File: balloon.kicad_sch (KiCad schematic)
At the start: 13 parts, among them SW1 SW_Push, U1 STM32L431RBTx, Y1 Crystal

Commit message: make board
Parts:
- added C1, C12, C13, C2: 100n, Capacitor_SMD:C_0603_1608Metric_Pad1.08x0.95mm_HandSolder, symbol Device:C
- added C14, C17: 4.7u, Capacitor_SMD:C_0603_1608Metric_Pad1.08x0.95mm_HandSolder, symbol Device:C
- added C5, C6: C, Capacitor_SMD:C_0603_1608Metric_Pad1.08x0.95mm_HandSolder, symbol Device:C
- added D1, D2: SK6812MINI, LED_SMD:LED_SK6812MINI_PLCC4_3.5x3.5mm_P1.75mm, symbol LED:SK6812MINI
- added J1: USB_B_Micro, Connector_USB:USB_Micro-B_Molex_47346-0001, symbol Connector:USB_B_Micro
- added J2, J3: Conn_01x06_Socket, Connector_PinHeader_2.54mm:PinHeader_1x06_P2.54mm_Vertical, symbol Connector:Conn_01x06_Socket
- added J4: Conn_01x02_Socket, Connector_PinHeader_2.54mm:PinHeader_1x02_P2.54mm_Vertical, symbol Connector:Conn_01x02_Socket
- added J5: Writing Connector, Connector_PinSocket_2.54mm:PinSocket_1x06_P2.54mm_Vertical, symbol Connector:Conn_01x06_Pin
- added R3: 10k, Resistor_SMD:R_0603_1608Metric_Pad0.98x0.95mm_HandSolder, symbol Device:R
- added R33, R34, R4: 2.2k, Resistor_SMD:R_0603_1608Metric_Pad0.98x0.95mm_HandSolder, symbol Device:R
- added U1: CH340N, Package_SO:MSOP-10_3x3mm_P0.5mm, symbol balloon_lib:CH340N
- added U2: Qwiic-SAM-M8Q, balloon:Qwiic_SAM-M8Q, symbol balloon_lib:Qwiic-SAM-M8Q
- added U3: AE_BME280, balloon:AE_BNE280, symbol balloon_lib:BME280
- added U4: AE_BNO055, balloon:AE-BNO055, symbol balloon_lib:BNO055
- added Y1: Crystal, Crystal:Crystal_C38-LF_D3.0mm_L8.0mm_Vertical, symbol Device:Crystal
- C10: renamed from C5; footprint (none) -> Capacitor_SMD:C_0603_1608Metric_Pad1.08x0.95mm_HandSolder
- C11: renamed from C9; footprint (none) -> Capacitor_SMD:C_0603_1608Metric_Pad1.08x0.95mm_HandSolder
- C3: renamed from C2; footprint (none) -> Capacitor_SMD:C_0603_1608Metric_Pad1.08x0.95mm_HandSolder
- C4: renamed from C3; footprint (none) -> Capacitor_SMD:C_0603_1608Metric_Pad1.08x0.95mm_HandSolder
- C7, C8: footprint (none) -> Capacitor_SMD:C_0603_1608Metric_Pad1.08x0.95mm_HandSolder; now not fitted
- C9: renamed from C4; footprint (none) -> Capacitor_SMD:C_0603_1608Metric_Pad1.08x0.95mm_HandSolder
- R1: renamed from R28; footprint (none) -> Resistor_SMD:R_0603_1608Metric_Pad0.98x0.95mm_HandSolder
- R2: renamed from R29; footprint (none) -> Resistor_SMD:R_0603_1608Metric_Pad0.98x0.95mm_HandSolder
- R5: renamed from R30; footprint (none) -> Resistor_SMD:R_0603_1608Metric_Pad0.98x0.95mm_HandSolder
- SW1: value SW_Push -> DTS-63-F-N-V-RED; footprint (none) -> Button_Switch_THT:SW_PUSH_6mm
- Y2: renamed from Y1; footprint (none) -> Crystal:Crystal_C38-LF_D3.0mm_L8.0mm_Vertical; now not fitted
- renumbered U1 to U5
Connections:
- net VMEM is gone; now on net +3V3: U5.1 (VBAT)
- net +3V3: now also C12.1, C14.1, C17.1, C2.1, D1.4 (VDD), D2.4 (VDD), J4.1 (Pin_1), R33.1, R34.1; no longer R1.1, R2.1
- net BNO055_RESET: now also U4.5 (RESET_N)
- net GND1: now also C1.2, C12.2, C13.2, C14.2, C17.2, C2.2, C5.1, C6.2, D1.2 (VSS), D2.2 (VSS), J1.5 (GND), J1.6 (Shield), J5.3 (Pin_3), R3.2, R4.2, U1.3 (GND), U2.13 (GND), U2.14 (GND), U2.5 (GND), U3.2 (GND), U4.2 (GND), U4.7 (GND); no longer SW1.1
- net GPS_INT: now also U2.4 (INT)
- net GPS_RESET: now also U2.2 (RST_N)
- net GPS_SAFE: now also U2.3 (SAFE_N)
- net I2C1_SCL: now also U4.4 (SCL/RX)
- net I2C1_SDA: now also U4.3 (SDA/TX)
- net LPTIM1_IN: now also U2.1 (PPS)
- net SPI1_CLK: now also U3.6 (SCK/SCL)
- net SPI1_MISO: now also U3.5 (MISO/GND)
- net SPI1_MOSI: now also U3.4 (MOSI/SDA)
- net SPI1_SS: now also U3.3 (CSB/VDD)
- net USART1_RX: now also U5.43 (PA10); no longer U5.59 (PB7)
- net USART3_RX: now also U2.10 (TXD)
- net USART3_TX: now also U2.11 (RXD)
- net NRST: now reaches R5.2, SW1.2, U5.7 (NRST)
- net NRST: now also C13.1, J5.5 (Pin_5)
- net PA0: now reaches U5.14 (PA0)
- net PA0: now also J3.3 (Pin_3)
- net USART2_TX: now reaches U5.16 (PA2)
- net USART2_TX: now also U1.7 (RXD)
- net USART2_RX: now reaches U5.17 (PA3)
- net USART2_RX: now also U1.6 (TXD)
- net CTRL_SENSE: now reaches U5.21 (PA5)
- net CTRL_COMM: now reaches U5.22 (PA6)
- net PA7: now reaches U5.23 (PA7)
- net PA7: now also J3.4 (Pin_4)
- net PB0: now reaches U5.26 (PB0)
- net PB0: now also J3.6 (Pin_6)
- net PB2: now reaches U5.28 (PB2)
- net PB2: now also J2.1 (Pin_1)
- net I2C2_SCL: now reaches U5.29 (PB10)
- net I2C2_SCL: now also R33.2
- net I2C2_SDA: now reaches U5.30 (PB11)
- net I2C2_SDA: now also R34.2
- net PB12: now reaches U5.33 (PB12)
- net PB12: now also J2.3 (Pin_3)
- net PB13: now reaches U5.34 (PB13)
- net PB13: now also J2.4 (Pin_4)
- net PB14: now reaches U5.35 (PB14)
- net PB14: now also J2.5 (Pin_5)
- net PB15: now reaches U5.36 (PB15)
- net PB15: now also J2.6 (Pin_6)
- net LED_OUT: now reaches U5.41 (PA8)
- net LED_OUT: now also D1.3 (DIN)
- net SWDIO: now reaches U5.46 (PA13)
- net SWDIO: now also J5.4 (Pin_4)
- net SWCLK: now reaches U5.49 (PA14)
- net SWCLK: now also J5.2 (Pin_2)
- net OSC_IN: now reaches U5.5 (PH0)
- net OSC_IN: now also C5.2, Y1.2
- net PA15: now reaches U5.50 (PA15)
- net PA15: now also J3.5 (Pin_5)
- net SWO: now reaches U5.55 (PB3)
- net SWO: now also J5.6 (Pin_6)
- net OSC_OUT: now reaches U5.6 (PH1)
- net OSC_OUT: now also C6.1, Y1.1
- net BOOT0: now reaches U5.60 (PH3)
- net BOOT0: now also J4.2 (Pin_2), R3.1
- net PC0: now reaches U5.8 (PC0)
- net PC0: now also J3.1 (Pin_1)
- net PC1: now reaches U5.9 (PC1)
- net PC1: now also J3.2 (Pin_2)
- new net: J1.2 (D-), U1.2 (UD-)
- new net: J1.3 (D+), U1.1 (UD+)
- new net: R4.1, SW1.1
- new net: C1.1, U1.8 (V3)
- new net: D1.1 (DOUT), D2.3 (DIN)
- new net +3.3V: J5.1 (Pin_1)
- new net PB7: J2.2 (Pin_2), U5.59 (PB7)
- new net PowerSource/5VIN: J1.1 (VBUS), U1.5 (~{CTS})
- new net PowerSource/VSENSE: R1.1, R2.1, U2.12 (3V3), U2.6 (3v3), U3.1 (VDD), U4.1 (VIN)
- no-connect marks 27 -> 8
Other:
- removed sheet BME280
- removed sheet BNO055
- removed sheet GPS
- sheet PowerSource ports: added 5VIN, CTRL_COMM, CTRL_SENSE, SCL, SDA, VCOMM, VSENSE, V_DEF; removed none
- sheet RM92A ports: added VIN; removed none
- sheet SDCard ports: added VIN; removed none
- moved on the sheet: C10, C11, C3, C4, C9, R1, R2, R5, SW1, U5

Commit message: replace PCB
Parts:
- added H1, H2, H3: MountingHole, MountingHole:MountingHole_3.2mm_M3_ISO7380, symbol Mechanical:MountingHole
- added J7: Conn_01x06_Socket, Connector_PinHeader_2.54mm:PinHeader_1x06_P2.54mm_Vertical, symbol Connector:Conn_01x06_Socket
- U1: footprint Package_SO:MSOP-10_3x3mm_P0.5mm -> Package_SO:SOP-8_3.9x4.9mm_P1.27mm
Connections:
- net +3V3: now also J3.6 (Pin_6), J7.6 (Pin_6)
- net GND1: now also J2.6 (Pin_6), J3.5 (Pin_5), J7.5 (Pin_5)
- net PA0: now also J2.3 (Pin_3); no longer J3.3 (Pin_3)
- net PA15: no longer J3.5 (Pin_5)
- net PA7: now also J2.4 (Pin_4); no longer J3.4 (Pin_4)
- net PB0: now also J2.5 (Pin_5); no longer J3.6 (Pin_6)
- net PB12 renamed SPI2_NSS
- net SPI2_NSS: now also J7.1 (Pin_1); no longer J2.3 (Pin_3)
- net PB13 renamed SPI2_SCK
- net SPI2_SCK: now also J7.4 (Pin_4); no longer J2.4 (Pin_4)
- net PB14 renamed SPI2_MISO
- net SPI2_MISO: now also J7.3 (Pin_3); no longer J2.5 (Pin_5)
- net PB15 renamed SPI2_MOSI
- net SPI2_MOSI: now also J7.2 (Pin_2); no longer J2.6 (Pin_6)
- net PC0 renamed I2C3_SCL
- net I2C3_SCL: now also J3.2 (Pin_2); no longer J3.1 (Pin_1)
- net PC1 renamed I2C3_SDA
- net I2C3_SDA: now also J3.1 (Pin_1); no longer J3.2 (Pin_2)
- no-connect marks 8 -> 10

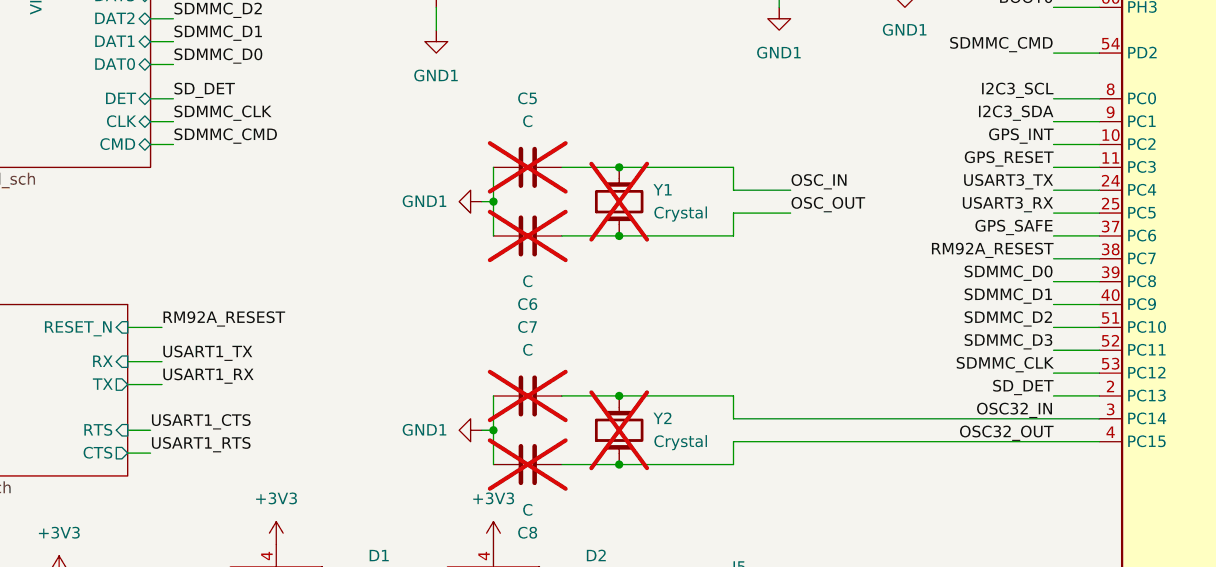
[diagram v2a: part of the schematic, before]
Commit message: add stmcube
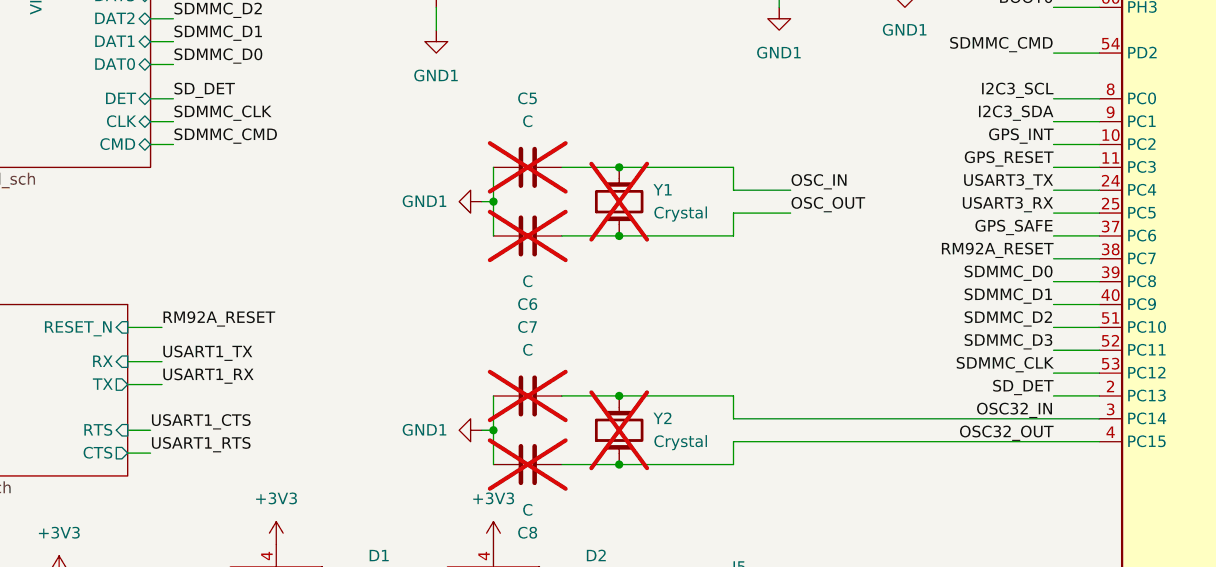
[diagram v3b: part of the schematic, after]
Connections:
- net RM92A_RESEST renamed RM92A_RESET

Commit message: change gnss
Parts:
- removed U2: Qwiic-SAM-M8Q, balloon:Qwiic_SAM-M8Q, symbol balloon_lib:Qwiic-SAM-M8Q
- added D7: D, Diode_SMD:D_SMA_Handsoldering, symbol Device:D
- added H4: MountingHole, MountingHole:MountingHole_3.2mm_M3_ISO7380, symbol Mechanical:MountingHole
- added R36: 1k, Resistor_SMD:R_0603_1608Metric_Pad0.98x0.95mm_HandSolder, symbol Device:R
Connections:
- net PowerSource/VSENSE renamed MAX-M10S/VIN
- net MAX-M10S/VIN: now also R36.2
- new net: D7.2 (A), R36.1
- new net MAX-M10S/VBKUP: D7.1 (K)
- no-connect marks 10 -> 8
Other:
- added sheet MAX-M10S (maxm10-s.kicad_sch)

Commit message: set gerber
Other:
- note added: "とりあえずブリッジさせる"
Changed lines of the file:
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@@
     (stroke (width 0) (type default))
+  )
+  (text "とりあえずブリッジさせる" (at 67.31 60.96 0)
+    (effects (font (size 1.27 1.27)) (justify left bottom))
   )
   (label "I2C1_SDA" (at 266.7 128.27 0) (fields_autoplaced)

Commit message: change schematics
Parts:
- H1, H2, H3, H4: footprint MountingHole:MountingHole_3.2mm_M3_ISO7380 -> MountingHole:MountingHole_3.2mm_M3_ISO7380_Pad_TopBottom; symbol Mechanical:MountingHole -> Mechanical:MountingHole_Pad
- SW1: footprint Button_Switch_THT:SW_PUSH_6mm -> Button_Switch_SMD:SW_SPST_PTS645
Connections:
- net GND1: now also H1.1, H2.1, H3.1, H4.1
- net USBD-: now reaches J1.2 (D-), U1.2 (UD-)
- net USBD+: now reaches J1.3 (D+), U1.1 (UD+)
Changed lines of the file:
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@@
   (junction (at 68.58 64.77) (diameter 0) (color 0 0 0 0)
   )
+  (junction (at 148.59 172.72) (diameter 0) (color 0 0 0 0)
+  )
+  (junction (at 148.59 167.64) (diameter 0) (color 0 0 0 0)
+  )
   (junction (at 73.66 171.45) (diameter 0) (color 0 0 0 0)
   )
@@
   )
   (junction (at 176.53 97.79) (diameter 0) (color 0 0 0 0)
+  )
+  (junction (at 148.59 162.56) (diameter 0) (color 0 0 0 0)
   )
   (junction (at 48.26 15.24) (diameter 0) (color 0 0 0 0)
@@
     (stroke (width 0) (type default))
   )
+  (wire (pts (xy 152.4 172.72) (xy 148.59 172.72))
+    (stroke (width 0) (type default))
+  )
   (wire (pts (xy 189.23 92.71) (xy 189.23 90.17))
     (stroke (width 0) (type default))
@@
     (stroke (width 0) (type default))
   )
+  (wire (pts (xy 148.59 162.56) (xy 148.59 157.48))
+    (stroke (width 0) (type default))
+  )
   (wire (pts (xy 114.3 195.58) (xy 116.84 195.58))
     (stroke (width 0) (type default))
@@
     (stroke (width 0) (type default))
   )
+  (wire (pts (xy 148.59 167.64) (xy 148.59 162.56))
+    (stroke (width 0) (type default))
+  )
   (wire (pts (xy 247.65 54.61) (xy 247.65 57.15))
     (stroke (width 0) (type default))
@@
     (stroke (width 0) (type default))
   )
+  (wire (pts (xy 148.59 172.72) (xy 148.59 167.64))
+    (stroke (width 0) (type default))
+  )
   (wire (pts (xy 247.65 20.32) (xy 260.35 20.32))
     (stroke (width 0) (type default))
@@
     (effects (font (size 1.27 1.27)) (justify right bottom))
   )
+  (label "USBD-" (at 29.21 35.56 0) (fields_autoplaced)
+    (effects (font (size 1.27 1.27)) (justify left bottom))
+  )
   (label "USART1_RTS" (at 266.7 92.71 0) (fields_autoplaced)
     (effects (font (size 1.27 1.27)) (justify left bottom))
@@
   )
   (label "NRST" (at 215.9 62.23 0) (fields_autoplaced)
+    (effects (font (size 1.27 1.27)) (justify left bottom))
+  )
+  (label "USBD+" (at 29.21 33.02 0) (fields_autoplaced)
     (effects (font (size 1.27 1.27)) (justify left bottom))
   )
@@
       (effects (font (size 1.27 1.27)))
     )
-    (property "Footprint" "Button_Switch_THT:SW_PUSH_6mm" (at 199.39 57.15 0)
+    (property "Footprint" "Button_Switch_SMD:SW_SPST_PTS645" (at 199.39 57.15 0)
       (effects (font (size 1.27 1.27)) hide)
     )
@@
     )
   )
-  (symbol (lib_id "Mechanical:MountingHole") (at 146.05 162.56 0) (unit 1)
-    (in_bom yes) (on_board yes) (dnp no) (fields_autoplaced)
-    (property "Reference" "H2" (at 148.59 161.3479 0)
-      (effects (font (size 1.27 1.27)) (justify left))
-    )
-    (property "Value" "MountingHole" (at 148.59 163.7721 0)
-      (effects (font (size 1.27 1.27)) (justify left))
-    )
-    (property "Footprint" "MountingHole:MountingHole_3.2mm_M3_ISO7380" (at 146.05 162.56 0)
+  (symbol (lib_id "Mechanical:MountingHole_Pad") (at 146.05 162.56 90) (unit 1)
+    (in_bom yes) (on_board yes) (dnp no)
+    (property "Reference" "H2" (at 140.97 161.29 90)
+      (effects (font (size 1.27 1.27)))
+    )
+    (property "Value" "MountingHole" (at 135.89 163.83 90)
+      (effects (font (size 1.27 1.27)))
+    )
+    (property "Footprint" "MountingHole:MountingHole_3.2mm_M3_ISO7380_Pad_TopBottom" (at 146.05 162.56 0)
       (effects (font (size 1.27 1.27)) hide)
     )
@@
       (effects (font (size 1.27 1.27)) hide)
     )
+    (pin "1")
     (instances
       (project "balloon"
@@
     )
   )
+  (symbol (lib_id "power:GND1") (at 152.4 172.72 0) (unit 1)
+    (in_bom yes) (on_board yes) (dnp no) (fields_autoplaced)
+    (property "Reference" "#PWR061" (at 152.4 179.07 0)
+      (effects (font (size 1.27 1.27)) hide)
+    )
+    (property "Value" "GND1" (at 152.4 177.8 0)
+      (effects (font (size 1.27 1.27)))
+    )
+    (property "Footprint" "" (at 152.4 172.72 0)
+      (effects (font (size 1.27 1.27)) hide)
+    )
+    (property "Datasheet" "" (at 152.4 172.72 0)
+      (effects (font (size 1.27 1.27)) hide)
+    )
+    (pin "1")
+    (instances
+      (project "balloon"
+        (path "/390c33b5-3f3b-4c86-a202-e8d785058178"
+          (reference "#PWR061") (unit 1)
+        )
+      )
+    )
+  )
   (symbol (lib_id "Device:C") (at 166.37 97.79 270) (mirror x) (unit 1)
     (in_bom yes) (on_board yes) (dnp yes)
@@
     )
   )
-  (symbol (lib_id "Mechanical:MountingHole") (at 146.05 172.72 0) (unit 1)
-    (in_bom yes) (on_board yes) (dnp no) (fields_autoplaced)
-    (property "Reference" "H4" (at 148.59 171.5079 0)
-      (effects (font (size 1.27 1.27)) (justify left))
-    )
-    (property "Value" "MountingHole" (at 148.59 173.9321 0)
-      (effects (font (size 1.27 1.27)) (justify left))
-    )
-    (property "Footprint" "MountingHole:MountingHole_3.2mm_M3_ISO7380" (at 146.05 172.72 0)
+  (symbol (lib_id "Mechanical:MountingHole_Pad") (at 146.05 172.72 90) (unit 1)
+    (in_bom yes) (on_board yes) (dnp no)
+    (property "Reference" "H4" (at 140.97 171.45 90)
+      (effects (font (size 1.27 1.27)))
+    )
+    (property "Value" "MountingHole" (at 135.89 173.99 90)
+      (effects (font (size 1.27 1.27)))
+    )
+    (property "Footprint" "MountingHole:MountingHole_3.2mm_M3_ISO7380_Pad_TopBottom" (at 146.05 172.72 0)
       (effects (font (size 1.27 1.27)) hide)
     )
@@
       (effects (font (size 1.27 1.27)) hide)
     )
+    (pin "1")
     (instances
       (project "balloon"
@@
     )
   )
-  (symbol (lib_id "Mechanical:MountingHole") (at 146.05 157.48 0) (unit 1)
-    (in_bom yes) (on_board yes) (dnp no) (fields_autoplaced)
-    (property "Reference" "H1" (at 148.59 156.2679 0)
-      (effects (font (size 1.27 1.27)) (justify left))
-    )
-    (property "Value" "MountingHole" (at 148.59 158.6921 0)
-      (effects (font (size 1.27 1.27)) (justify left))
-    )
-    (property "Footprint" "MountingHole:MountingHole_3.2mm_M3_ISO7380" (at 146.05 157.48 0)
+  (symbol (lib_id "Mechanical:MountingHole_Pad") (at 146.05 157.48 90) (unit 1)
+    (in_bom yes) (on_board yes) (dnp no)
+    (property "Reference" "H1" (at 140.97 156.21 90)
+      (effects (font (size 1.27 1.27)))
+    )
+    (property "Value" "MountingHole" (at 135.89 158.75 90)
+      (effects (font (size 1.27 1.27)))
+    )
+    (property "Footprint" "MountingHole:MountingHole_3.2mm_M3_ISO7380_Pad_TopBottom" (at 146.05 157.48 0)
       (effects (font (size 1.27 1.27)) hide)
     )
@@
       (effects (font (size 1.27 1.27)) hide)
     )
+    (pin "1")
     (instances
       (project "balloon"
@@
     )
   )
-  (symbol (lib_id "Mechanical:MountingHole") (at 146.05 167.64 0) (unit 1)
-    (in_bom yes) (on_board yes) (dnp no) (fields_autoplaced)
-    (property "Reference" "H3" (at 148.59 166.4279 0)
-      (effects (font (size 1.27 1.27)) (justify left))
-    )
-    (property "Value" "MountingHole" (at 148.59 168.8521 0)
-      (effects (font (size 1.27 1.27)) (justify left))
-    )
-    (property "Footprint" "MountingHole:MountingHole_3.2mm_M3_ISO7380" (at 146.05 167.64 0)
+  (symbol (lib_id "Mechanical:MountingHole_Pad") (at 146.05 167.64 90) (unit 1)
+    (in_bom yes) (on_board yes) (dnp no)
+    (property "Reference" "H3" (at 140.97 166.37 90)
+      (effects (font (size 1.27 1.27)))
+    )
+    (property "Value" "MountingHole" (at 135.89 168.91 90)
+      (effects (font (size 1.27 1.27)))
+    )
+    (property "Footprint" "MountingHole:MountingHole_3.2mm_M3_ISO7380_Pad_TopBottom" (at 146.05 167.64 0)
       (effects (font (size 1.27 1.27)) hide)
     )
@@
       (effects (font (size 1.27 1.27)) hide)
     )
-    (instances
-      (project "balloon"
+    (pin "1")
+    (instances
+      (project "balloon"
